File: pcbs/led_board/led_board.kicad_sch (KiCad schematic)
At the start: 4 parts, among them J1 CONN HEADER R/A 2POS 1.5MM, U1 1.4-40V PWM Dimmer 100mA

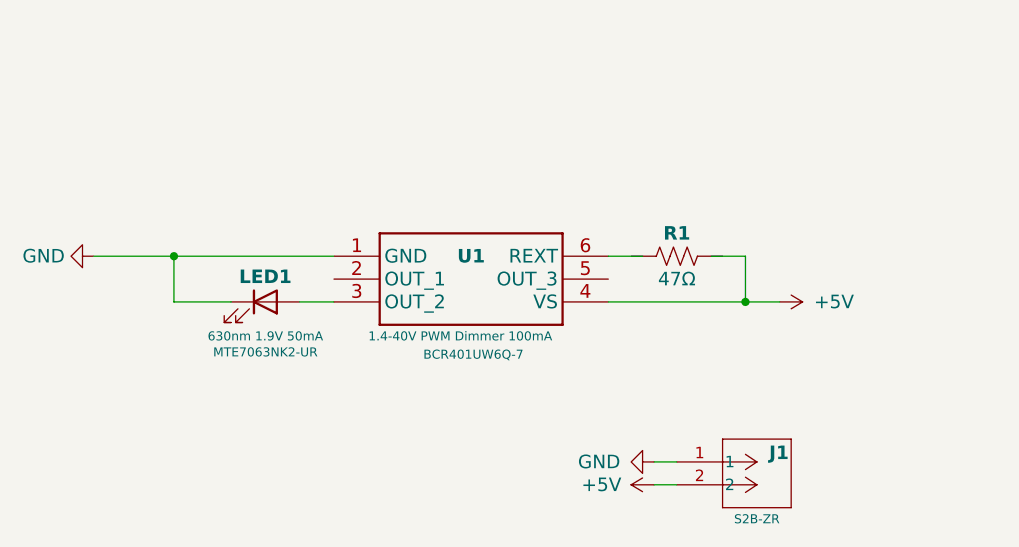
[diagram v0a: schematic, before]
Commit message: update led board to version 1.0 (just text upates)
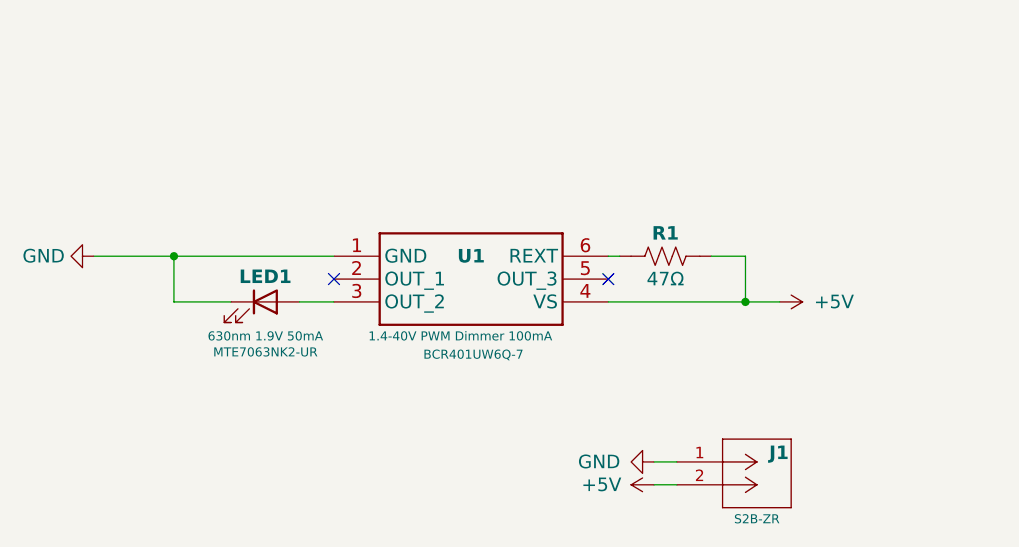
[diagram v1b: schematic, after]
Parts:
- R1: JLCPCB (none) -> C3008836; JLCPCBURL (none) -> https://jlcpcb.com/partdetail/VishayIntertech-CRCW120647R0F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
- U1: JLCPCB (none) -> C2678813; JLCPCBURL (none) -> https://jlcpcb.com/partdetail/DiodesIncorporated-BCR401UW6Q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
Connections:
- net +5V: now also R1.2
- net at R1.1: now also U1.6 (REXT)
- no-connect marks 0 -> 2
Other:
- moved on the sheet: R1
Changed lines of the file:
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@@
 		(color 0 0 0 0)
+	)
+	(no_connect
+		(at 134.62 96.52)
+	)
+	(no_connect
+		(at 165.1 96.52)
 	)
 	(wire
@@
 	(wire
 		(pts
+			(xy 165.1 93.98) (xy 166.37 93.98)
+		)
+		(stroke
+			(width 0)
+			(type default)
+		)
+	)
+	(wire
+		(pts
 			(xy 123.19 99.06) (xy 116.84 99.06)
 		)
@@
 		(pts
 			(xy 176.53 93.98) (xy 180.34 93.98)
-		)
-		(stroke
-			(width 0.1524)
-			(type solid)
-		)
-	)
-	(wire
-		(pts
-			(xy 165.1 93.98) (xy 168.91 93.98)
 		)
 		(stroke
@@
 	(symbol
 		(lib_id "symbols:R_US")
-		(at 172.72 93.98 180)
+		(at 171.45 93.98 180)
 		(unit 1)
 		(exclude_from_sim no)
@@
 		(dnp no)
 		(property "Reference" "R1"
-			(at 172.72 91.44 0)
+			(at 171.45 91.44 0)
 			(effects
 				(font
@@
 		)
 		(property "Value" "47Ω"
-			(at 172.72 96.52 0)
+			(at 171.45 96.52 0)
 			(effects
 				(font
@@
 		)
 		(property "Footprint" "footprints:R_1206"
-			(at 171.704 93.726 90)
+			(at 170.434 93.726 90)
 			(effects
 				(font
@@
 		)
 		(property "Datasheet" "~"
-			(at 172.72 93.98 0)
+			(at 171.45 93.98 0)
 			(effects
 				(font
@@
 		)
 		(property "Description" "Resistor, US symbol"
-			(at 172.72 93.98 0)
+			(at 171.45 93.98 0)
+			(effects
+				(font
+					(size 1.27 1.27)
+				)
+				(hide yes)
+			)
+		)
+		(property "JLCPCB" "C3008836"
+			(at 171.45 93.98 0)
+			(effects
+				(font
+					(size 1.27 1.27)
+				)
+				(hide yes)
+			)
+		)
+		(property "JLCPCBURL" "https://jlcpcb.com/partdetail/VishayIntertech-CRCW120647R0FKEAHP/C3008836"
+			(at 171.45 93.98 0)
 			(effects
 				(font
@@
 			(at 134.62 93.98 0)
 			(effects
+				(font
+					(size 1.27 1.27)
+				)
+				(hide yes)
+			)
+		)
+		(property "JLCPCB" "C2678813"
+			(at 134.62 93.98 0)
+			(effects
+				(font
+					(size 1.27 1.27)
+				)
+				(hide yes)
+			)
+		)
+		(property "JLCPCBURL" "https://jlcpcb.com/partdetail/DiodesIncorporated-BCR401UW6Q7/C2678813"
+			(at 134.62 93.98 0)
+			(effects

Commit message: update LED board with multiple resistor options
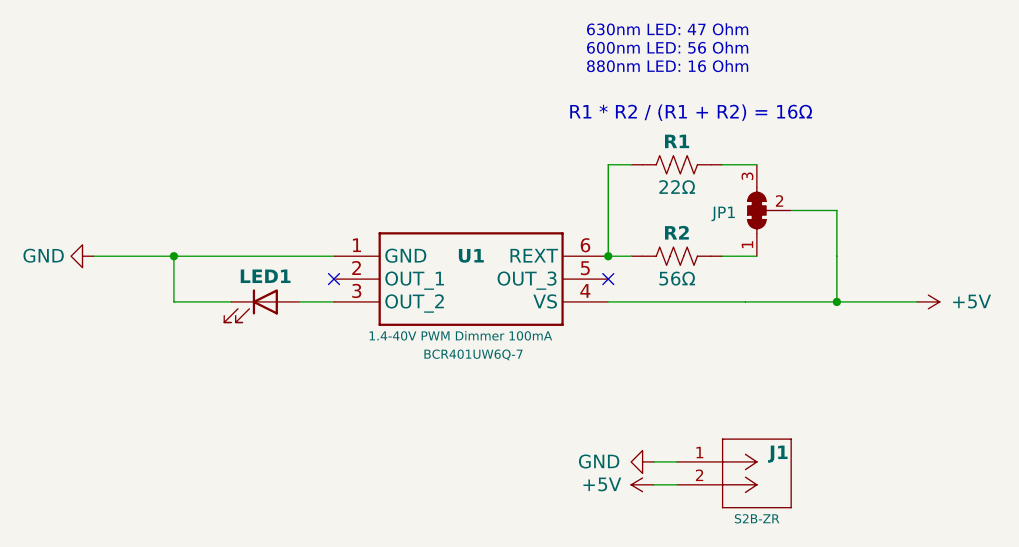
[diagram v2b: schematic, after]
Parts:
- added JP1: SolderJumper_3_Bridged123, footprints:SolderJumper3_Bridged, symbol symbols:SolderJumper_3_Bridged123
- added R2: 56Ω, footprints:R_1206, symbol symbols:R_US
- R1: value 47Ω -> 22Ω; JLCPCB C3008836 -> C17958; JLCPCBURL https://jlcpcb.com/partdetail/VishayIntertech-CRCW120647R0F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 -> https://jlcpcb.com/partdetail/18646-1206W4F220JT5E/C17958
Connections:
- net +5V: now also JP1.2 (C); no longer R1.2
- net at R1.1, U1.6 (REXT): now also R2.1
- new net: JP1.3 (B), R1.2
- new net: JP1.1 (A), R2.2
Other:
- note added: "630nm LED: 47 Ohm 600nm LED: 56 Ohm 880nm LED: 16 Ohm"
- note added: "R1 * R2 / (R1 + R2) = 16Ω"
- moved on the sheet: R1
